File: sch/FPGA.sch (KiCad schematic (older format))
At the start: 15 parts, among them U2 iCE40-HX8K-CT256, U3 N25Q032A13EF440F, Y1 ECS-5032MV-120-BM-TR

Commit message: Add voltage regulator
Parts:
- Y1: footprint ECS5032MV120BMTR -> ECS-5032MV-120-BM-TR:ECS5032MV120BMTR
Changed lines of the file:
@@
 F 0 "Y1" H 3200 7215 50  0000 C CNN
 F 1 "ECS-5032MV-120-BM-TR" H 3200 7124 50  0000 C CNN
-F 2 "ECS5032MV120BMTR" H 3800 7050 50  0001 L CNN
+F 2 "ECS-5032MV-120-BM-TR:ECS5032MV120BMTR" H 3800 7050 50  0001 L CNN
 F 3 "https://www.arrow.com/en/products/ecs-5032mv-120-bm-tr/ecs-international" H 3800 6950 50  0001 L CNN
 F 4 "Standard Clock Oscillators 12MHz 1.8-3.3V 50ppm -20C +70C" H 3800 6850 50  0001 L CNN "Description"

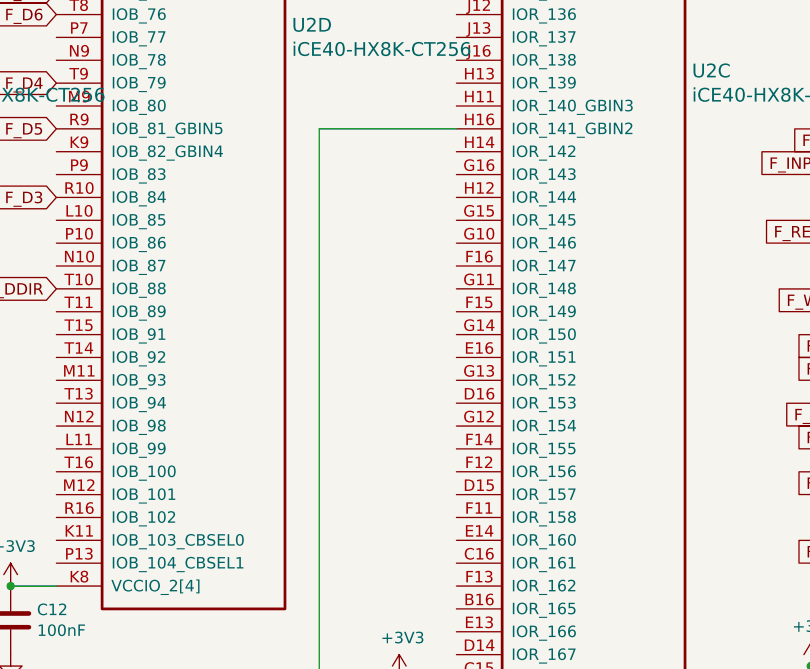
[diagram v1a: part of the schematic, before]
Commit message: Add usb controller
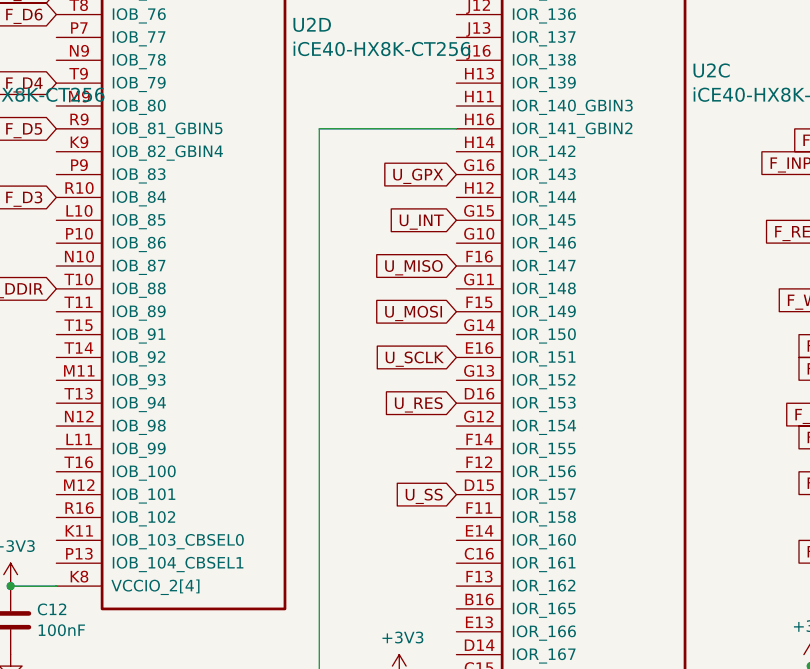
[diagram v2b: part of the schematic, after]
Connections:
- net U_SS: now reaches U2.D15 (IOR_157)
- net U_RES: now reaches U2.D16 (IOR_153)
- net U_SCLK: now reaches U2.E16 (IOR_151)
- net U_MOSI: now reaches U2.F15 (IOR_149)
- net U_MISO: now reaches U2.F16 (IOR_147)
- net U_INT: now reaches U2.G15 (IOR_145)
- net U_GPX: now reaches U2.G16 (IOR_143)
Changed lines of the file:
@@
 F1 "pwr.sch" 50
 $EndSheet
+Text GLabel 5150 4550 0    50   Input ~ 0
+U_MOSI
+Text GLabel 5150 4350 0    50   Input ~ 0
+U_MISO
+Text GLabel 5150 5350 0    50   Input ~ 0
+U_SS
+Text GLabel 5150 4750 0    50   Input ~ 0
+U_SCLK
+Text GLabel 5150 4950 0    50   Input ~ 0
+U_RES
+Text GLabel 5150 4150 0    50   Input ~ 0
+U_INT
+Text GLabel 5150 3950 0    50   Input ~ 0
+U_GPX
 $EndSCHEMATC

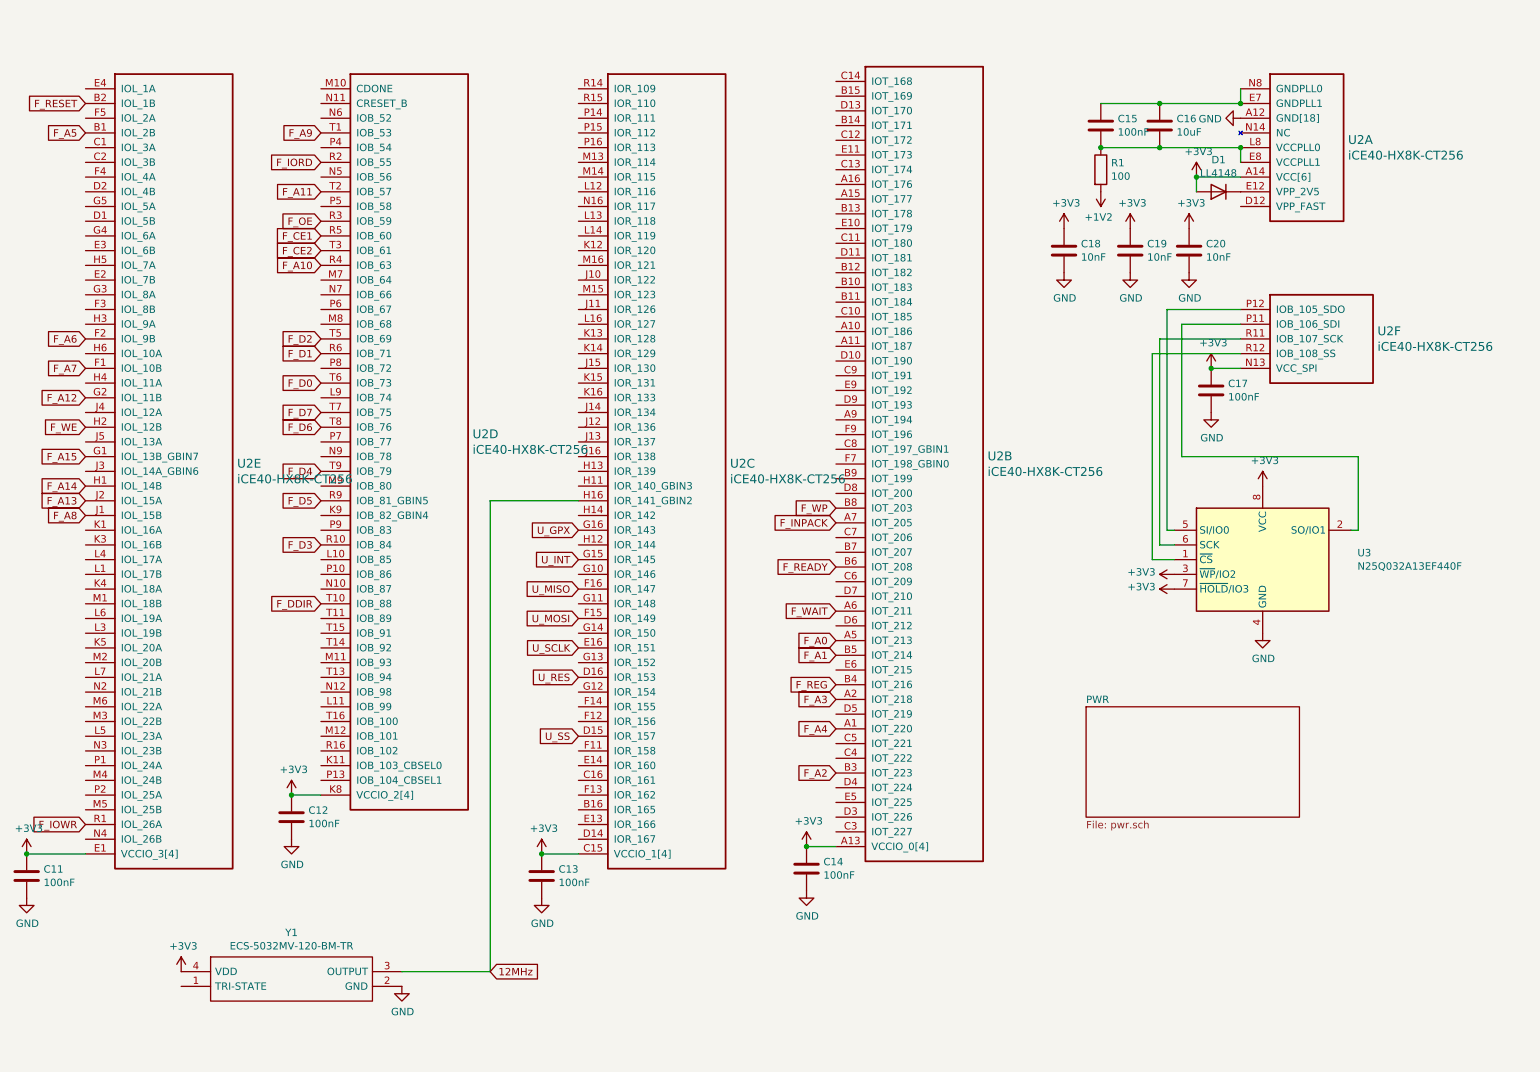
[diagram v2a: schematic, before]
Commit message: Add programming connector
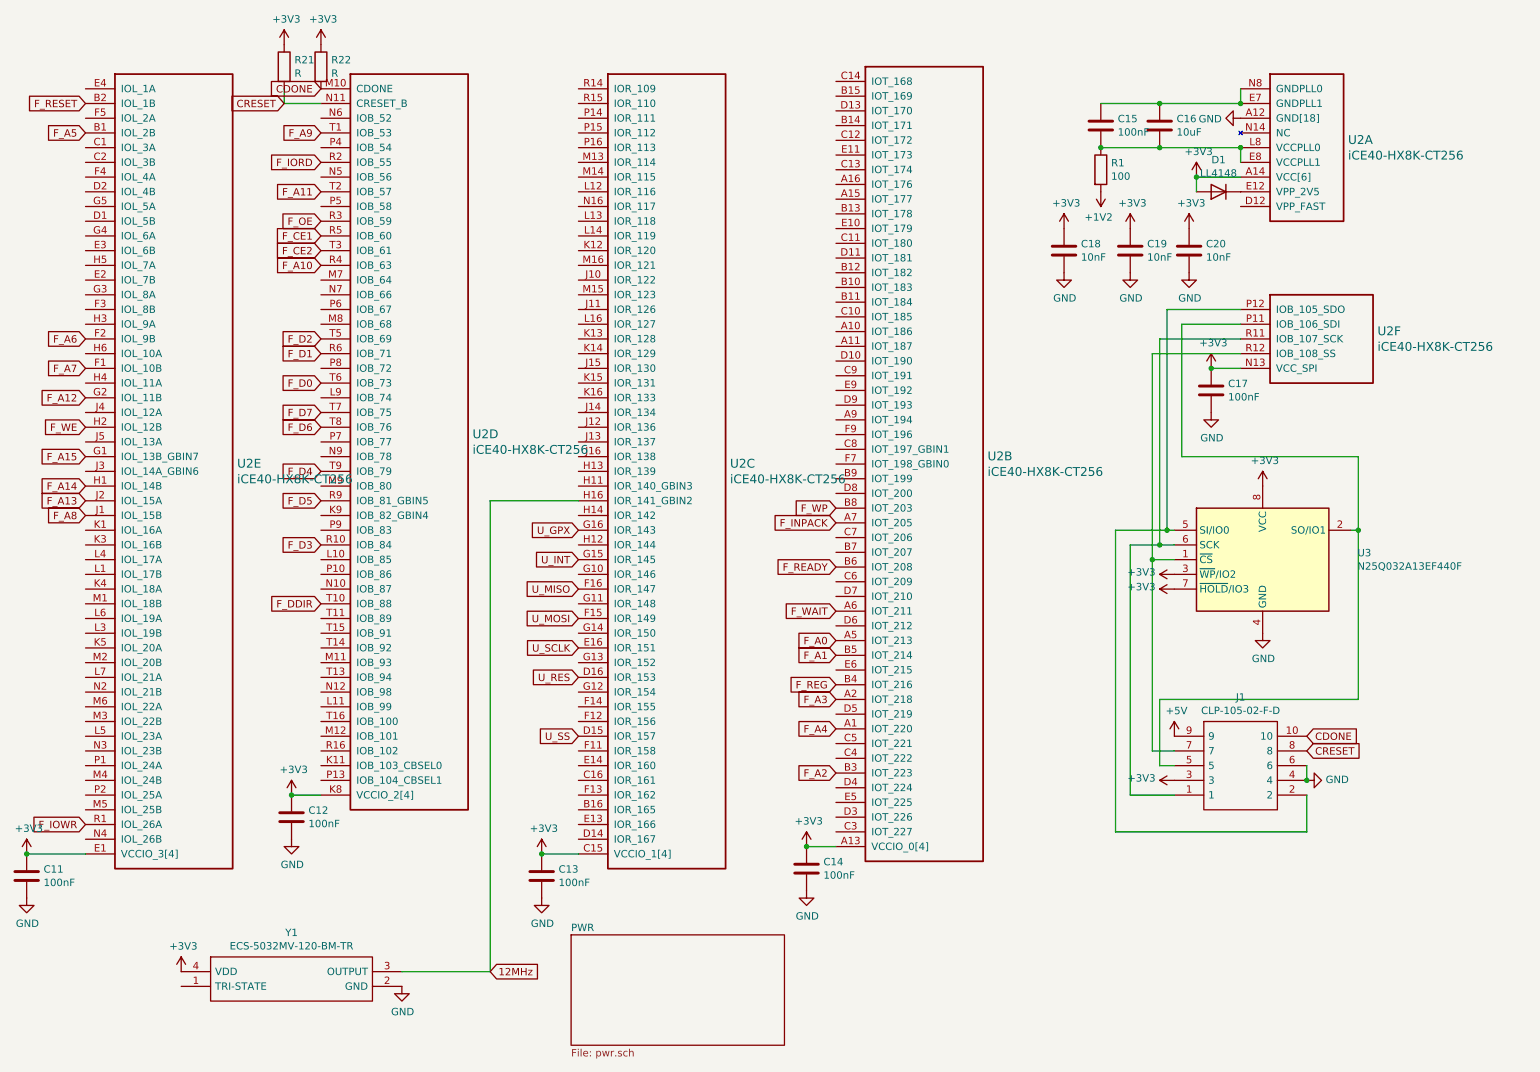
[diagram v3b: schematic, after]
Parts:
- added J1: CLP-105-02-F-D, CLP-105-02-F-D:CLP-105-02-XXX-D, symbol CLP-105-02-F-D:CLP-105-02-F-D
- added R21, R22: R, Resistor_SMD:R_0402_1005Metric, symbol Device:R
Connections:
- net +3V3: now also J1.3, R21.1, R22.1
- net GND: now also J1.4, J1.6
- net CDONE: now reaches U2.M10 (CDONE)
- net CDONE: now also J1.10, R22.2
- net CRESET: now reaches U2.N11 (CRESET_B)
- net CRESET: now also J1.8, R21.2
- net at U2.P11 (IOB_106_SDI), U3.2 (SO/IO1): now also J1.5
- net at U2.P12 (IOB_105_SDO), U3.5 (SI/IO0): now also J1.2
- net at U2.R11 (IOB_107_SCK), U3.6 (SCK): now also J1.1
- net at U2.R12 (IOB_108_SS), U3.1 (~CS): now also J1.7
- new net +5V: J1.9
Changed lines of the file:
@@
 12MHz
 $Sheet
-S 8600 5150 1450 750
+S 5100 6700 1450 750
 U 60E6B938
 F0 "PWR" 50
@@
 Text GLabel 5150 3950 0    50   Input ~ 0
 U_GPX
+$Comp
+L CLP-105-02-F-D:CLP-105-02-F-D J1
+U 1 1 60FC32F7
+P 9200 5350
+F 0 "J1" H 9650 5615 50  0000 C CNN
+F 1 "CLP-105-02-F-D" H 9650 5524 50  0000 C CNN
+F 2 "CLP-105-02-F-D:CLP-105-02-XXX-D" H 9950 5450 50  0001 L CNN
+F 3 "http://suddendocs.samtec.com/prints/erm8-xxx-xx.x-xxx-dv-xxxx-xx-mkt.pdf" H 9950 5350 50  0001 L CNN
+F 4 "10 Position Connector Header, Center Strip Contacts Surface Mount" H 9950 5250 50  0001 L CNN "Description"
+F 5 "" H 9950 5150 50  0001 L CNN "Height"
+F 6 "SAMTEC" H 9950 5050 50  0001 L CNN "Manufacturer_Name"
+F 7 "CLP-105-02-F-D" H 9950 4950 50  0001 L CNN "Manufacturer_Part_Number"
+F 8 "200-CLP10502FD" H 9950 4850 50  0001 L CNN "Mouser Part Number"
+F 9 "https://www.mouser.co.uk/ProductDetail/Samtec/CLP-105-02-F-D?qs=2tpXfLKpFkhlColP9v%252BhkA%3D%3D" H 9950 4750 50  0001 L CNN "Mouser Price/Stock"
+F 10 "CLP-105-02-F-D" H 9950 4650 50  0001 L CNN "Arrow Part Number"
+F 11 "https://www.arrow.com/en/products/clp-105-02-f-d/samtec" H 9950 4550 50  0001 L CNN "Arrow Price/Stock"
+	1    9200 5350
+	1    0    0    -1
+$EndComp
+Wire Wire Line
+	9150 3950 8800 3950
+Wire Wire Line
+	8800 3950 8800 6000
+Wire Wire Line
+	8800 6000 10100 6000
+Wire Wire Line
+	10100 6000 10100 5750
+Connection ~ 9150 3950
+Wire Wire Line
+	9100 4050 8900 4050
+Wire Wire Line
+	8900 4050 8900 5750
+Wire Wire Line
+	8900 5750 9200 5750
+Connection ~ 9100 4050
+$Comp
+L power:+3V3 #PWR0195
+U 1 1 6103CF53
+P 9200 5650
+F 0 "#PWR0195" H 9200 5500 50  0001 C CNN
+F 1 "+3V3" V 9215 5778 50  0000 L CNN
+F 2 "" H 9200 5650 50  0001 C CNN
+F 3 "" H 9200 5650 50  0001 C CNN
+	1    9200 5650
+	0    -1   -1   0
+$EndComp
+Wire Wire Line
+	10450 3950 10450 5100
+Wire Wire Line
+	10450 5100 9100 5100
+Wire Wire Line
+	9100 5100 9100 5550
+Wire Wire Line
+	9100 5550 9200 5550
+Connection ~ 10450 3950
+Wire Wire Line
+	9050 4150 9050 5450
+Wire Wire Line
+	9050 5450 9200 5450
+Connection ~ 9050 4150
+$Comp
+L power:+5V #PWR0196
+U 1 1 61049926
+P 9200 5350
+F 0 "#PWR0196" H 9200 5200 50  0001 C CNN
+F 1 "+5V" H 9215 5523 50  0000 C CNN
+F 2 "" H 9200 5350 50  0001 C CNN
+F 3 "" H 9200 5350 50  0001 C CNN
+	1    9200 5350
+	1    0    0    -1
+$EndComp
+$Comp
+L power:GND #PWR0197
+U 1 1 6104A693
+P 10100 5650
+F 0 "#PWR0197" H 10100 5400 50  0001 C CNN
+F 1 "GND" V 10105 5522 50  0000 R CNN
+F 2 "" H 10100 5650 50  0001 C CNN
+F 3 "" H 10100 5650 50  0001 C CNN
+	1    10100 5650
+	0    -1   -1   0
+$EndComp
+$Comp
+L Device:R R22
+U 1 1 6105683F
+P 3400 800
+F 0 "R22" H 3470 846 50  0000 L CNN
+F 1 "R" H 3470 755 50  0000 L CNN
+F 2 "Resistor_SMD:R_0402_1005Metric" V 3330 800 50  0001 C CNN
+F 3 "~" H 3400 800 50  0001 C CNN
+	1    3400 800
+	1    0    0    -1
+$EndComp
+$Comp
+L Device:R R21
+U 1 1 61057B92
+P 3150 800
+F 0 "R21" H 3220 846 50  0000 L CNN
+F 1 "R" H 3220 755 50  0000 L CNN
+F 2 "Resistor_SMD:R_0402_1005Metric" V 3080 800 50  0001 C CNN
+F 3 "~" H 3150 800 50  0001 C CNN
+	1    3150 800
+	1    0    0    -1
+$EndComp
+$Comp
+L power:+3V3 #PWR021
+U 1 1 61058AAB
+P 3150 650
+F 0 "#PWR021" H 3150 500 50  0001 C CNN
+F 1 "+3V3" H 3165 823 50  0000 C CNN
+F 2 "" H 3150 650 50  0001 C CNN
+F 3 "" H 3150 650 50  0001 C CNN
+	1    3150 650
+	1    0    0    -1
+$EndComp
+$Comp
+L power:+3V3 #PWR022
+U 1 1 610599A2
+P 3400 650
+F 0 "#PWR022" H 3400 500 50  0001 C CNN
+F 1 "+3V3" H 3415 823 50  0000 C CNN
+F 2 "" H 3400 650 50  0001 C CNN
+F 3 "" H 3400 650 50  0001 C CNN
+	1    3400 650
+	1    0    0    -1
+$EndComp
+Wire Wire Line
+	3400 1050 3150 1050
+Wire Wire Line
+	3150 1050 3150 950
+Text GLabel 3400 950  0    50   Input ~ 0
+CDONE
+Text GLabel 3150 1050 0    50   Input ~ 0
+CRESET
+Text GLabel 10100 5450 2    50   Input ~ 0
+CRESET
+Text GLabel 10100 5350 2    50   Input ~ 0
+CDONE
+Wire Wire Line
+	10100 5550 10100 5650
+Connection ~ 10100 5650
 $EndSCHEMATC

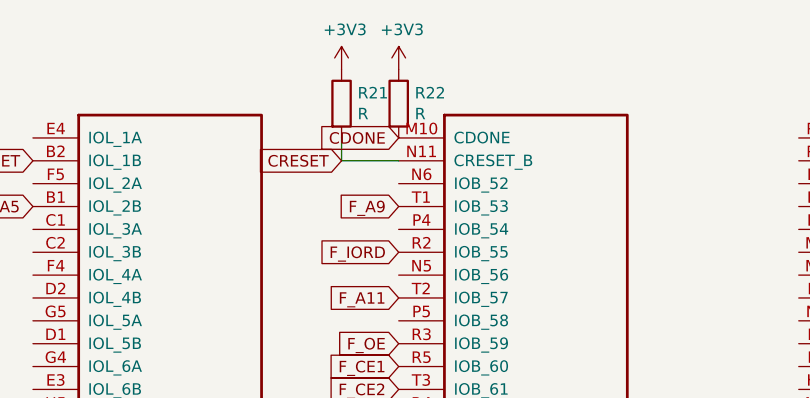
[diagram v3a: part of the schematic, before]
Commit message: Add proper value of resistors
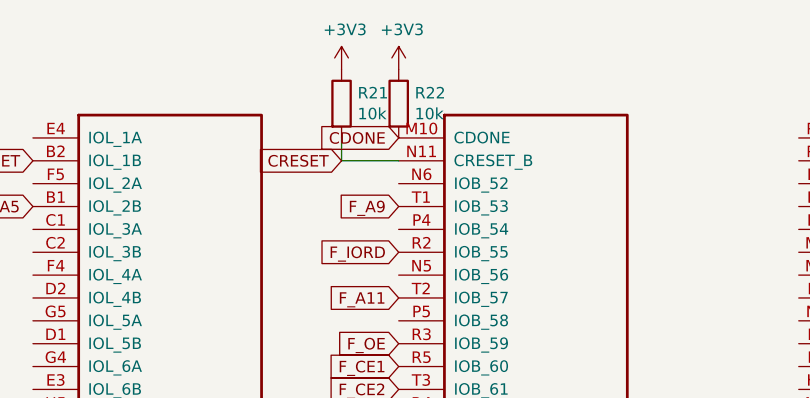
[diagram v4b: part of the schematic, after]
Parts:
- R21, R22: value R -> 10k
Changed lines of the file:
@@
 P 3400 800
 F 0 "R22" H 3470 846 50  0000 L CNN
-F 1 "R" H 3470 755 50  0000 L CNN
+F 1 "10k" H 3470 755 50  0000 L CNN
 F 2 "Resistor_SMD:R_0402_1005Metric" V 3330 800 50  0001 C CNN
 F 3 "~" H 3400 800 50  0001 C CNN
@@
 P 3150 800
 F 0 "R21" H 3220 846 50  0000 L CNN
-F 1 "R" H 3220 755 50  0000 L CNN
+F 1 "10k" H 3220 755 50  0000 L CNN
 F 2 "Resistor_SMD:R_0402_1005Metric" V 3080 800 50  0001 C CNN
 F 3 "~" H 3150 800 50  0001 C CNN

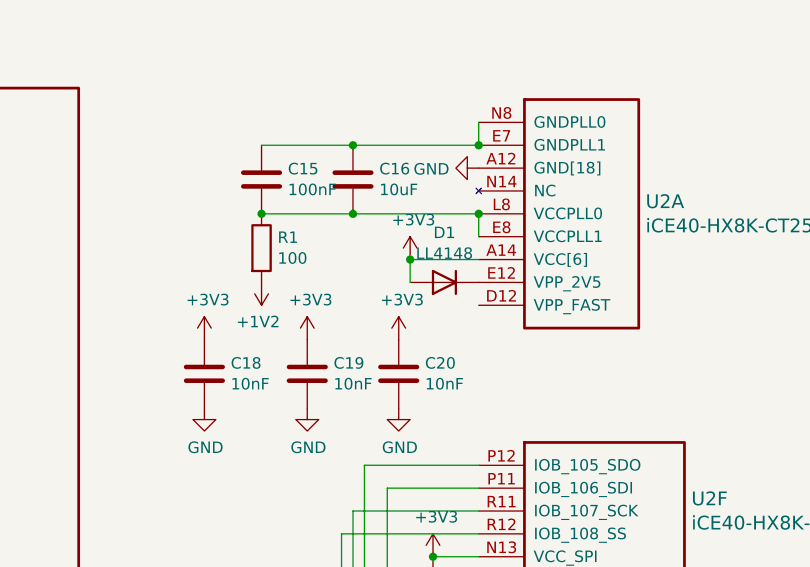
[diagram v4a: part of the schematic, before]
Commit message: Replace diode
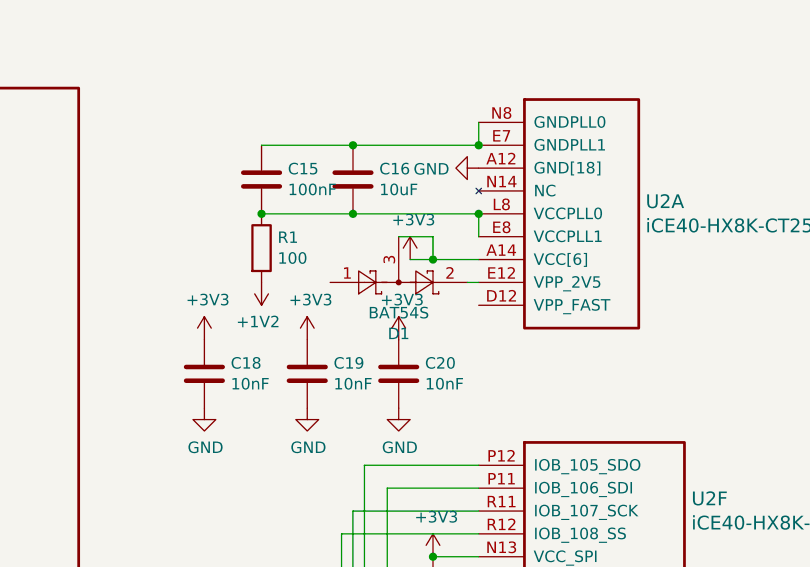
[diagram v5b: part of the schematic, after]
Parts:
- removed D1: LL4148, Diode_SMD:D_MiniMELF, symbol Diode:LL4148
- added D1: BAT54S, Package_TO_SOT_SMD:SOT-23, symbol Diode:BAT54S
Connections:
- net +3V3: now also D1.3
- net at U2.E12 (VPP_2V5): now also D1.2
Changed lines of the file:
@@
 	9050 4150 9200 4150
-$Comp
-L Diode:LL4148 D1
-U 1 1 60B8313E
-P 9500 1650
-F 0 "D1" H 9500 1433 50  0000 C CNN
-F 1 "LL4148" H 9500 1524 50  0000 C CNN
-F 2 "Diode_SMD:D_MiniMELF" H 9500 1475 50  0001 C CNN
-F 3 "http://www.vishay.com/docs/85557/ll4148.pdf" H 9500 1650 50  0001 C CNN
-	1    9500 1650
-	-1   0    0    1
-$EndComp
 $Comp
 L power:+3V3 #PWR0163
@@
 $EndComp
 Wire Wire Line
-	9650 1550 9350 1550
-Wire Wire Line
-	9350 1650 9350 1550
-Connection ~ 9350 1550
+	9650 1550 9450 1550
 Wire Wire Line
 	9650 1450 9650 1350
@@
 	10100 5550 10100 5650
 Connection ~ 10100 5650
+$Comp
+L Diode:BAT54S D1
+U 1 1 6083AC98
+P 9300 1650
+F 0 "D1" H 9300 1875 50  0000 C CNN
+F 1 "BAT54S" H 9300 1784 50  0000 C CNN
+F 2 "Package_TO_SOT_SMD:SOT-23" H 9375 1775 50  0001 L CNN
+F 3 "https://www.diodes.com/assets/Datasheets/ds11005.pdf" H 9180 1650 50  0001 C CNN
+	1    9300 1650
+	1    0    0    1
+$EndComp
+Wire Wire Line
+	9300 1450 9450 1450
+Wire Wire Line
+	9450 1450 9450 1550
+Connection ~ 9450 1550
+Wire Wire Line
+	9450 1550 9350 1550
+Wire Wire Line
+	9600 1650 9650 1650
 $EndSCHEMATC
